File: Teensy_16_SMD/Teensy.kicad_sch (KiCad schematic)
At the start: 3 parts, among them J20 RJ45_LED, U1 Teensy4.1

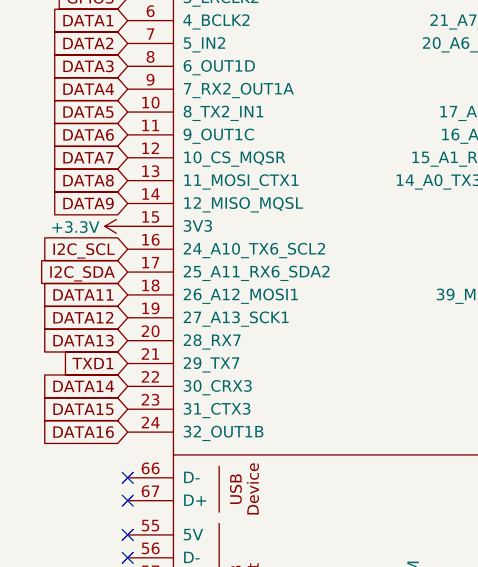
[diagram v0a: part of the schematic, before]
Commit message: added PCB for walmart tree
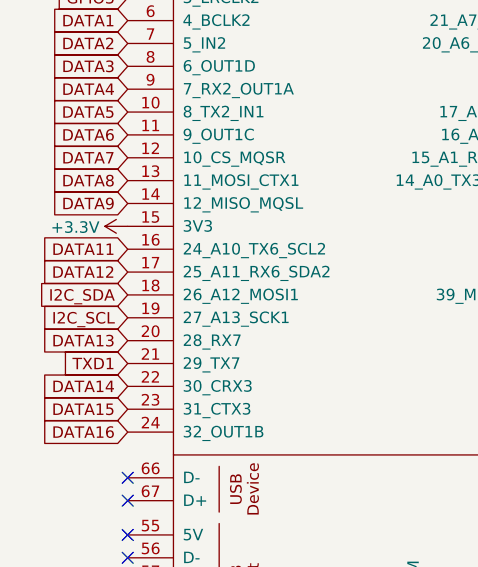
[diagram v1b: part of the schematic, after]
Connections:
- net DATA11: now also U1.16 (24_A10_TX6_SCL2); no longer U1.18 (26_A12_MOSI1)
- net DATA12: now also U1.17 (25_A11_RX6_SDA2); no longer U1.19 (27_A13_SCK1)
- net I2C_SCL: now also U1.19 (27_A13_SCK1); no longer U1.16 (24_A10_TX6_SCL2)
- net I2C_SDA: now also U1.18 (26_A12_MOSI1); no longer U1.17 (25_A11_RX6_SDA2)
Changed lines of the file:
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@@
     )
   )
-  (global_label "I2C_SDA" (shape input) (at 114.3 91.44 180) (fields_autoplaced)
+  (global_label "I2C_SDA" (shape input) (at 114.3 93.98 180) (fields_autoplaced)
     (effects (font (size 1.27 1.27)) (justify right))
-    (property "Intersheet References" "${INTERSHEET_REFS}" (id 0) (at 320.04 167.64 0)
+    (property "Intersheet References" "${INTERSHEET_REFS}" (id 0) (at 320.04 170.18 0)
       (effects (font (size 1.27 1.27)) hide)
     )
@@
     )
   )
-  (global_label "DATA12" (shape input) (at 114.3 96.52 180) (fields_autoplaced)
+  (global_label "DATA12" (shape input) (at 114.3 91.44 180) (fields_autoplaced)
     (effects (font (size 1.27 1.27)) (justify right))
-    (property "Intersheet References" "${INTERSHEET_REFS}" (id 0) (at 241.3 162.56 0)
+    (property "Intersheet References" "${INTERSHEET_REFS}" (id 0) (at 241.3 157.48 0)
       (effects (font (size 1.27 1.27)) hide)
     )
@@
     )
   )
-  (global_label "DATA11" (shape input) (at 114.3 93.98 180) (fields_autoplaced)
+  (global_label "DATA11" (shape input) (at 114.3 88.9 180) (fields_autoplaced)
     (effects (font (size 1.27 1.27)) (justify right))
-    (property "Intersheet References" "${INTERSHEET_REFS}" (id 0) (at 33.02 27.94 0)
+    (property "Intersheet References" "${INTERSHEET_REFS}" (id 0) (at 33.02 22.86 0)
       (effects (font (size 1.27 1.27)) hide)
     )
@@
     )
   )
-  (global_label "I2C_SCL" (shape input) (at 114.3 88.9 180) (fields_autoplaced)
+  (global_label "I2C_SCL" (shape input) (at 114.3 96.52 180) (fields_autoplaced)
     (effects (font (size 1.27 1.27)) (justify right))
-    (property "Intersheet References" "${INTERSHEET_REFS}" (id 0) (at -45.72 12.7 0)
+    (property "Intersheet References" "${INTERSHEET_REFS}" (id 0) (at -45.72 20.32 0)
       (effects (font (size 1.27 1.27)) hide)
     )
